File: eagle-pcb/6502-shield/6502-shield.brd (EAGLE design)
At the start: 101.6 x 53.3 mm, 38 parts

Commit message: Bunch of work on rev b. but more to do.
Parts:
- added C10, C11, C12, C13, C14, C15, C16, C17, C18, C19, C20, C21, C22, C23, C24, C25, C26, C27, C28, C8, C9: 0.1uF, rcl:C0805
- added U1, U2, U3, U4, U5, U6: TCB0108-LVL-XLTRTSSOP20, 6502-shield:SOP65P640X120-20N
- C1, C2, C3, C4, C5, C6, C7: device rcl:C0402 -> rcl:C0805
- R18, R2, R3, R4, R5, R6, R7, R8, R9: device rcl:R0402 -> rcl:R0603
- moved JP2 75.4 mm to (11.2, 10.0), turned to 0 degrees
- moved C7 71.6 mm to (3.30, 46.6), turned to 180 degrees
- moved J1 47.2 mm to (2.75, 50.1), turned to 270 degrees
- moved PIO 45.3 mm to (39.1, 15.1), turned to 45 degrees
- moved SW_RUNHALT 42.6 mm to (5.80, 4.65), turned to 0 degrees
- moved C6 42.0 mm to (16.0, 17.5), turned to 225 degrees
- moved RAM 41.3 mm to (74.2, 18.5)
- moved JP3 39.9 mm to (71.1, 47.6), turned to 180 degrees
- moved JP1 39.0 mm to (8.90, 50.4)
- moved C5 38.7 mm to (9.55, 24.0), turned to 225 degrees
- moved PB_STEP 38.5 mm to (20.6, 4.10)
- moved R19 36.8 mm to (70.0, 43.4), turned to 270 degrees
- moved FPGA 36.3 mm to (20.1, 28.9), turned to 45 degrees
- moved EXT_XO 34.4 mm to (8.90, 41.0), turned to 270 degrees
- moved R3 32.0 mm to (15.8, 45.0)
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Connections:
- new net A0_IO: PCB1.44, U2.20
- new net A10_IO: PCB1.34, U1.17
- new net A11_IO: PCB1.35, U1.16
- new net A12_IO: PCB1.32, U1.15
- new net A13_IO: PCB1.33, U1.14
- new net A14_IO: PCB1.30, U1.13
- new net A15_IO: PCB1.31, U1.12
- new net A1_IO: PCB1.45, U2.18
- new net A2_IO: PCB1.42, U2.17
- new net A3_IO: PCB1.43, U2.16
- new net A4_IO: PCB1.40, U2.15
- new net A5_IO: PCB1.41, U2.14
- new net A6_IO: PCB1.38, U2.13
- new net A7_IO: PCB1.39, U2.12
- new net A8_IO: PCB1.36, U1.20
- new net A9_IO: PCB1.37, U1.18
- new net CLK_IO: PCB1.27, U6.15
- new net D0_IO: PCB1.52, U3.20
- new net D1_IO: PCB1.53, U3.18
- new net D2_IO: PCB1.50, U3.17
- new net D3_IO: PCB1.51, U3.16
- new net D4_IO: PCB1.48, U3.15
- new net D5_IO: PCB1.49, U3.14
- new net D6_IO: PCB1.46, U3.13
- new net D7_IO: PCB1.47, U3.12
- new net DMA_IO: PCB1.22, U6.14
- new net EEPROM_PGM_IO: PCB1.23, U6.18
- new net IRQ_COPROC: FPGA.7, U6.4
- new net IRQ_COPROC_IO: PCB1.24, U6.17
- new net IRQ_IO: FPGA.8, PIO.17
- new net OE_IO: PCB1.25, U6.20
- new net PA0_IO: JP2.1, U4.12
- new net PA1_IO: JP2.3, U4.13
- new net PA2_IO: JP2.5, U4.14
- new net PA3_IO: JP2.7, U4.15
- new net PA4_IO: JP2.9, U4.16
- new net PA5_IO: JP2.11, U4.17
- new net PA6_IO: JP2.13, U4.18
- new net PA7_IO: JP2.15, U4.20
- new net PB0_IO: JP2.2, U5.12
- new net PB1_IO: JP2.4, U5.13
- new net PB2_IO: JP2.6, U5.14
- new net PB3_IO: JP2.8, U5.15
- new net PB4_IO: JP2.10, U5.16
- new net PB5_IO: JP2.12, U5.17
- new net PB6_IO: JP2.14, U5.18
- new net PB7_IO: JP2.16, U5.20
- new net VCCIO: C14.1, C15.1, C16.1, C17.1, C18.1, C19.1, JP3.1, PCB1.5V, PCB1.5V., PCB1.5V.., U1.19, U2.19, U3.19, U4.19, U5.19, U6.19
- new net WE_IO: PCB1.29, U6.16
- net A0: now also U2.1; no longer PCB1.44
- net A1: now also U2.3; no longer PCB1.45
- net A10: now also U1.4; no longer PCB1.34
- net A11: now also U1.5; no longer PCB1.35
- net A12: now also U1.6; no longer PCB1.32
- net A13: now also U1.7; no longer PCB1.33
- net A14: now also U1.8; no longer PCB1.30
- net A15: now also U1.9; no longer PCB1.31
- net A2: now also U2.4; no longer PCB1.42
- net A3: now also U2.5; no longer PCB1.43
- net A4: now also U2.6; no longer PCB1.40
- net A5: now also U2.7; no longer PCB1.41
- net A6: now also U2.8; no longer PCB1.38
- net A7: now also U2.9; no longer PCB1.39
- net A8: now also U1.1; no longer PCB1.36
- net A9: now also U1.3; no longer PCB1.37
- net CLK: now also U6.6; no longer PCB1.27
- net D0: now also U3.1; no longer PCB1.52
- net D1: now also U3.3; no longer PCB1.53
- net D2: now also U3.4; no longer PCB1.50
- net D3: now also U3.5; no longer PCB1.51
- net D4: now also U3.6; no longer PCB1.48
- net D5: now also U3.7; no longer PCB1.49
- net D6: now also U3.8; no longer PCB1.46
- net D7: now also U3.9; no longer PCB1.47
- net DMA: now also U6.7; no longer PCB1.22
- net EEPROM_PGM: now also U6.3; no longer PCB1.23
- net GND: now also C10.2, C11.2, C12.2, C13.2, C14.2, C15.2, C16.2, C17.2, C18.2, C19.2, C20.2, C21.2, C22.2, C23.2, C24.2, C25.2, C26.2, C27.2, C28.2, C8.2, C9.2, U1.11, U2.11, U3.11, U4.11, U5.11, U6.11, U6.8, U6.9
- net IRQN: no longer PIO.17
- net OE: now also U6.1; no longer PCB1.25
- net PA0: now also U4.9; no longer JP2.1
- net PA1: now also U4.8; no longer JP2.3
- net PA2: now also U4.7; no longer JP2.5
- net PA3: now also U4.6; no longer JP2.7
- net PA4: now also U4.5; no longer JP2.9
- net PA5: now also U4.4; no longer JP2.11
- net PA6: now also U4.3; no longer JP2.13
- net PA7: now also U4.1; no longer JP2.15
- net PB0: now also U5.9; no longer JP2.2
- net PB1: now also U5.8; no longer JP2.4
- net PB2: now also U5.7; no longer JP2.6
- net PB3: now also U5.6; no longer JP2.8
- net PB4: now also U5.5; no longer JP2.10
- net PB5: now also U5.4; no longer JP2.12
- net PB6: now also U5.3; no longer JP2.14
- net PB7: now also U5.1; no longer JP2.16
- net TCK: now also JP1.4; no longer JP1.6
- net TDI: now also JP1.3; no longer JP1.4
- net TMS: now also JP1.6; no longer JP1.3
- net VCC: now also C10.1, C11.1, C12.1, C13.1, C20.1, C21.1, C22.1, C23.1, C24.1, C25.1, C26.1, C27.1, C28.1, C8.1, C9.1, U1.10, U1.2, U2.10, U2.2, U3.10, U3.2, U4.10, U4.2, U5.10, U5.2, U6.10, U6.2; no longer JP3.1
- net WE: now also U6.5; no longer PCB1.29
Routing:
- net IRQN: track 175.5 -> 0.00 mm, vias 4 -> 0
- net CLK: track 155.5 -> 0.00 mm, vias 4 -> 0
- net EEPROM_PGM: track 149.6 -> 0.00 mm, vias 2 -> 0
- net DMA: track 134.7 -> 0.00 mm, vias 2 -> 0
- net RW: track 129.1 -> 0.00 mm, vias 3 -> 0
- net VCCIO: track 0.00 -> 124.8 mm, vias 0 -> 1
- net D0: track 122.1 -> 0.00 mm, vias 5 -> 0
- net A10: track 121.4 -> 0.00 mm, vias 4 -> 0
- net D1: track 116.5 -> 0.00 mm, vias 5 -> 0
- net A13: track 116.3 -> 0.00 mm, vias 4 -> 0
- net WE: track 113.3 -> 0.00 mm, vias 3 -> 0
- net D2: track 110.7 -> 0.00 mm, vias 5 -> 0
- net A3: track 110.2 -> 0.00 mm, vias 5 -> 0
- net A14: track 107.8 -> 0.00 mm, vias 4 -> 0
- net A15: track 107.2 -> 0.00 mm, vias 2 -> 0
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- removed copper zone on layer 1, net GND
- removed copper zone on layer 16, net GND

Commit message: More routing work on the pcb, lots more left... yay =/
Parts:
- moved U5 15.7 mm to (29.7, 7.28), turned to 0 degrees
- moved U4 14.6 mm to (29.6, 16.5)
- moved C18 6.90 mm to (23.5, 18.8), turned to 0 degrees
- moved C19 5.94 mm to (23.5, 9.43), turned to 0 degrees
- moved C11 3.39 mm to (36.0, 18.8), turned to 180 degrees
- moved C13 2.43 mm to (36.0, 9.59), turned to 180 degrees
- moved JP2 1.85 mm to (11.1, 11.9), turned to 180 degrees
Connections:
- net CLK: now also U6.3; no longer U6.6
- net CLK_IO: now also U6.18; no longer U6.15
- net EEPROM_PGM: now also U6.6; no longer U6.3
- net EEPROM_PGM_IO: now also U6.15; no longer U6.18
- net IRQ_COPROC: now also U6.5; no longer U6.4
- net IRQ_COPROC_IO: now also U6.16; no longer U6.17
- net OE: now also U6.4; no longer U6.1
- net OE_IO: now also U6.17; no longer U6.20
- net PB0: now also U5.1; no longer U5.9
- net PB0_IO: now also U5.20; no longer U5.12
- net PB1: now also U5.3; no longer U5.8
- net PB1_IO: now also U5.18; no longer U5.13
- net PB2: now also U5.4; no longer U5.7
- net PB2_IO: now also U5.17; no longer U5.14
- net PB3: now also U5.5; no longer U5.6
- net PB3_IO: now also U5.16; no longer U5.15
- net PB4: now also U5.6; no longer U5.5
- net PB4_IO: now also U5.15; no longer U5.16
- net PB5: now also U5.7; no longer U5.4
- net PB5_IO: now also U5.14; no longer U5.17
- net PB6: now also U5.8; no longer U5.3
- net PB6_IO: now also U5.13; no longer U5.18
- net PB7: now also U5.9; no longer U5.1
- net PB7_IO: now also U5.12; no longer U5.20
- net WE: now also U6.1; no longer U6.5
- net WE_IO: now also PCB1.28, U6.20; no longer PCB1.29, U6.16
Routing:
- net VCC: track 388.3 -> 500.4 mm, vias 5 -> 13
- net VCCIO: track 124.8 -> 173.8 mm, vias 1 -> 4
- net IRQ_IO: track 0.00 -> 39.3 mm, vias 0 -> 2
- net PB_STEP: track 0.00 -> 32.9 mm
- net PA7_IO: track 0.00 -> 27.6 mm
- net PB7_IO: track 0.00 -> 27.4 mm
- net PB6_IO: track 0.00 -> 24.3 mm
- net SW_RUNHALT: track 0.00 -> 24.1 mm
- net PA6_IO: track 0.00 -> 24.1 mm
- net PB5_IO: track 0.00 -> 21.3 mm
- net PA5_IO: track 0.00 -> 21.3 mm
- net PB4_IO: track 0.00 -> 18.8 mm
- net PA4_IO: track 0.00 -> 18.5 mm
- net PB3_IO: track 0.00 -> 16.3 mm
- net PA3_IO: track 0.00 -> 15.6 mm
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
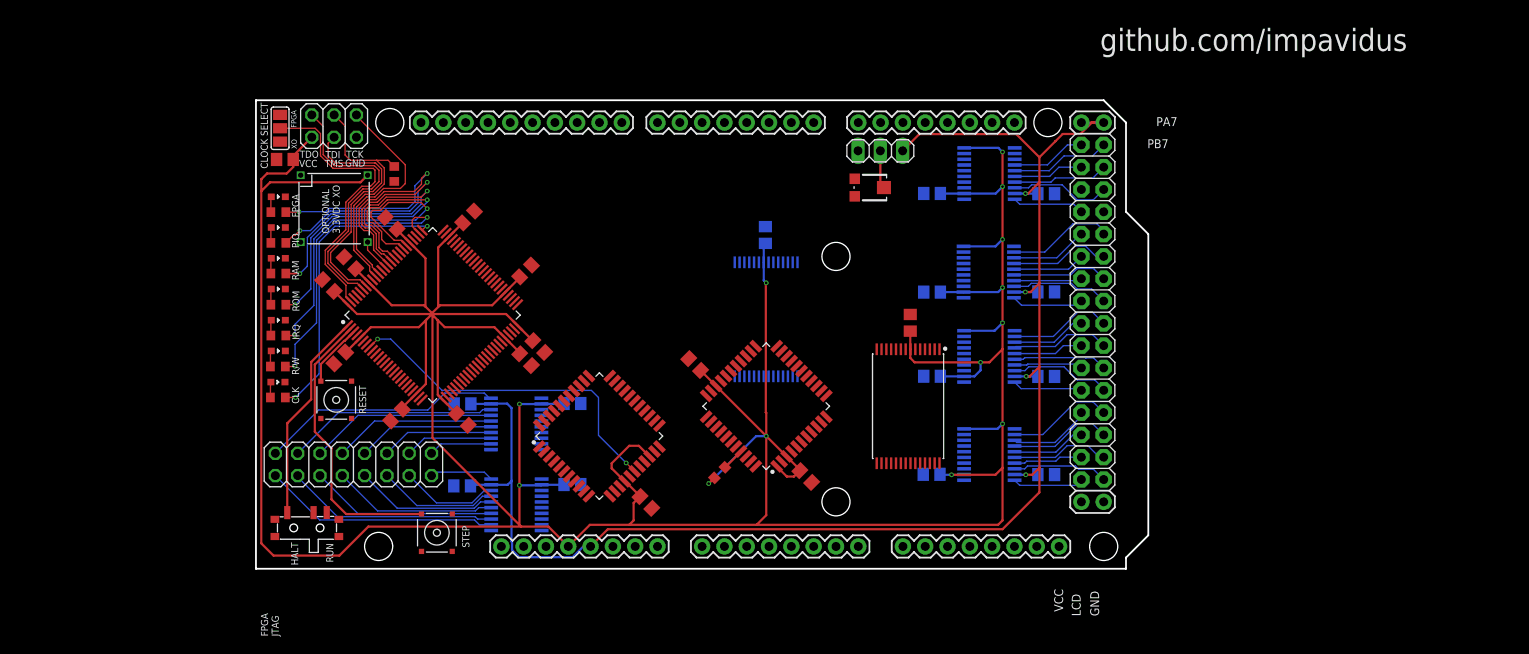
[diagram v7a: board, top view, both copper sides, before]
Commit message: The fpga is now fully broken out and mostly routed, edges of board are routed so pretty much just the busses left to do.
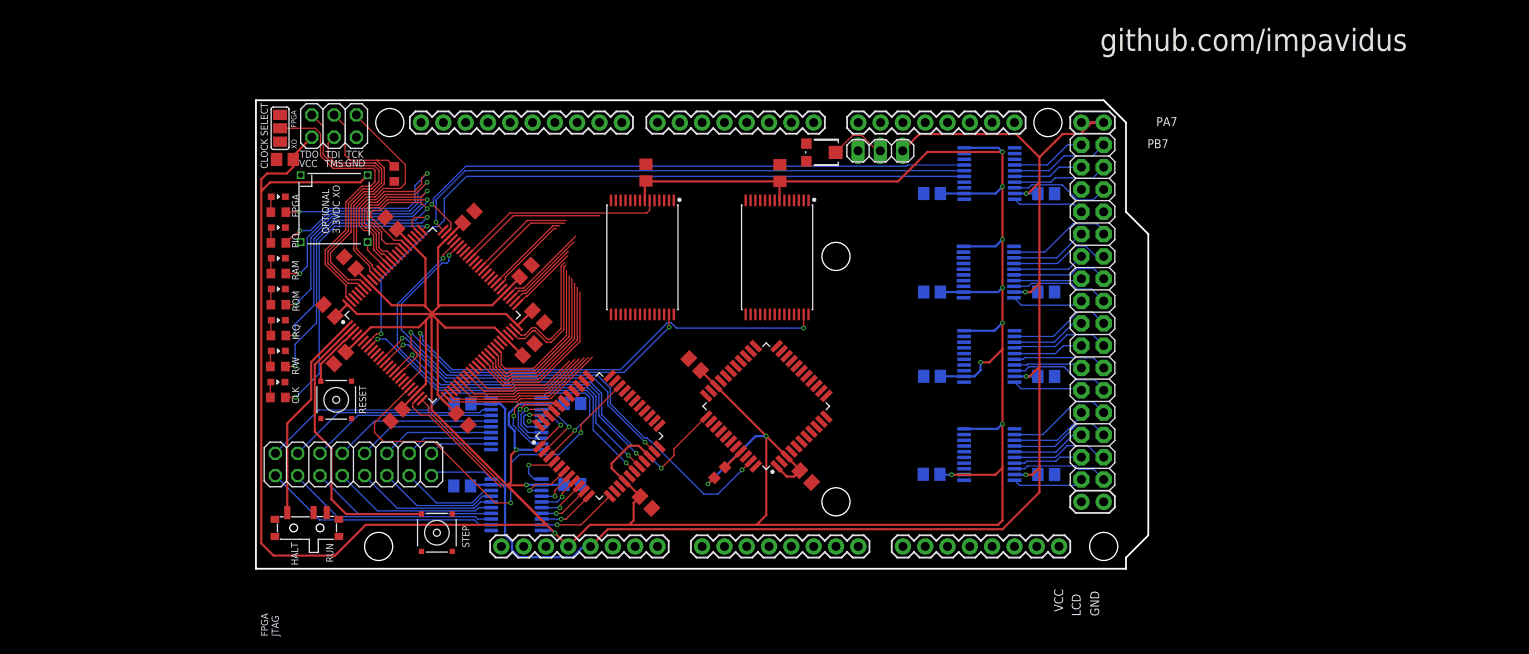
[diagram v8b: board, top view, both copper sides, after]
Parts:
- moved RAM 34.7 mm to (44.0, 35.5)
- moved C27 22.6 mm to (59.6, 45.0)
- moved C28 15.3 mm to (44.4, 45.1), flipped to the top
- moved EEPROM 7.16 mm to (59.3, 35.5), flipped to the top
- moved R19 6.80 mm to (64.5, 47.4)
- moved C22 3.40 mm to (32.1, 28.7)
- moved C23 2.85 mm to (8.35, 29.4)
- moved C21 1.20 mm to (31.1, 24.9), turned to 45 degrees
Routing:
- net IRQ_COPROC: track 0.00 -> 81.1 mm, vias 0 -> 1
- net DMA: track 0.00 -> 67.2 mm, vias 0 -> 1
- net EEPROM_PGM: track 0.00 -> 65.3 mm, vias 0 -> 1
- net IRQN: track 0.00 -> 62.8 mm, vias 0 -> 2
- net ROM_EN: track 0.00 -> 56.3 mm, vias 0 -> 2
- net RW: track 0.00 -> 49.6 mm, vias 0 -> 2
- net BE: track 0.00 -> 47.5 mm, vias 0 -> 2
- net RESETN: track 0.00 -> 46.7 mm, vias 0 -> 2
- net RAM_EN: track 0.00 -> 41.0 mm, vias 0 -> 2
- net CLK: track 0.00 -> 38.3 mm, vias 0 -> 2
- net IO_EN: track 0.00 -> 35.9 mm, vias 0 -> 2
- net WE: track 0.00 -> 23.9 mm
- net VCC: track 500.4 -> 524.0 mm
- net A0: track 0.00 -> 20.1 mm
- net A1: track 0.00 -> 20.0 mm
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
